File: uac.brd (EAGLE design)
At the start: 160 x 100 mm, 158 parts, among them Q1 2N7002CK4SST

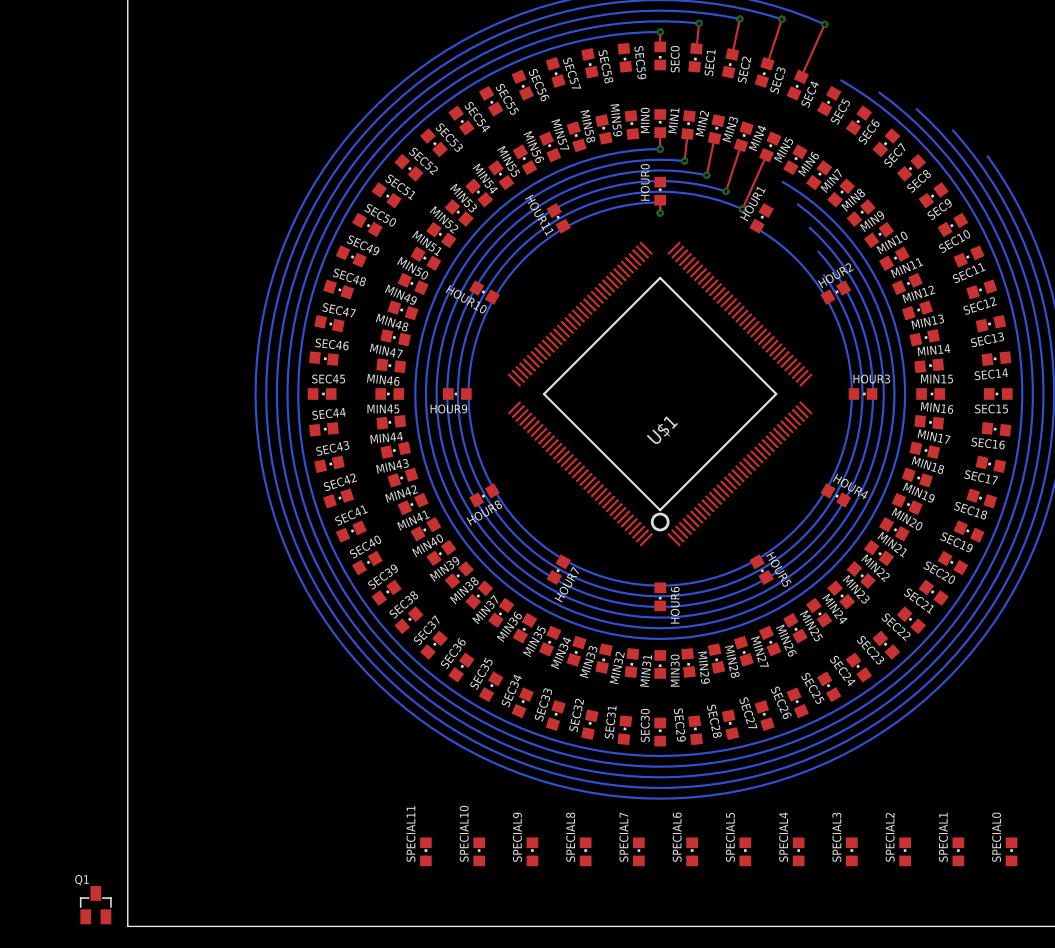
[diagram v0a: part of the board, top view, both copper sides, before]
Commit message: Arcdozen 2 toegevoegd
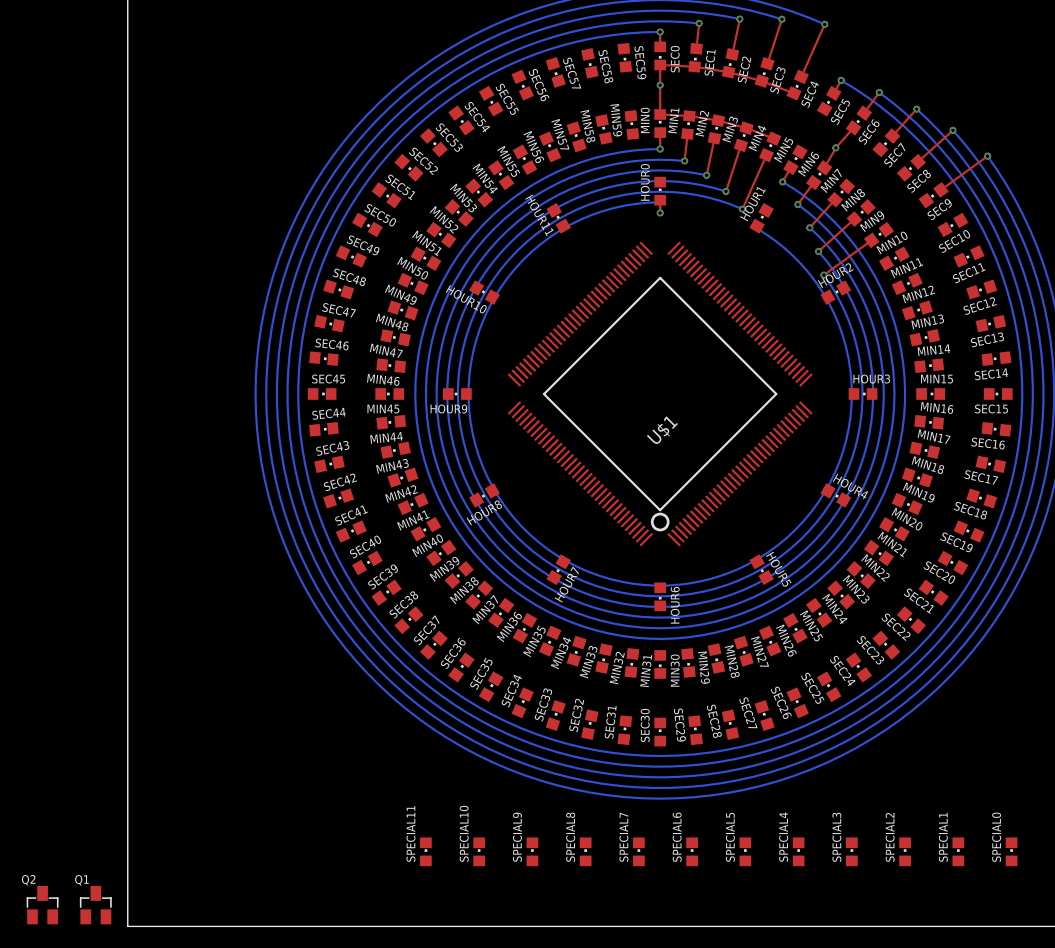
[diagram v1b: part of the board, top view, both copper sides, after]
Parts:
- added Q2: 2N7002CK4SST, Custom components:SOT23
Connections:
- new net ARCDOZEN_2: Q2.1
- new net N$1: HOUR1.C, MIN5.C, MIN6.C, MIN7.C, MIN8.C, MIN9.C, Q2.3, SEC5.C, SEC6.C, SEC7.C, SEC8.C, SEC9.C, SPECIAL1.C
- net DOZEN1: now also HOUR1.A
- net DOZEN10: now also SEC8.A
- net DOZEN11: now also SEC9.A
- net DOZEN12: now also SPECIAL1.A
- net DOZEN2: now also MIN5.A
- net DOZEN3: now also MIN6.A
- net DOZEN4: now also MIN7.A
- net DOZEN5: now also MIN8.A
- net DOZEN6: now also MIN9.A
- net DOZEN7: now also SEC5.A
- net DOZEN8: now also SEC6.A
- net DOZEN9: now also SEC7.A
- net GND: now also Q2.2
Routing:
- net N$3: track 0.00 -> 28.6 mm, vias 0 -> 1
- net DOZEN6: track 15.4 -> 20.9 mm, vias 1 -> 2
- net DOZEN11: track 25.1 -> 30.5 mm, vias 1 -> 2
- net N$1: track 0.00 -> 4.67 mm, vias 0 -> 1
- net DOZEN5: track 14.9 -> 19.5 mm, vias 1 -> 2
- net DOZEN10: track 23.6 -> 28.0 mm, vias 1 -> 2
- net DOZEN4: track 14.4 -> 18.0 mm, vias 1 -> 2
- net DOZEN9: track 22.0 -> 25.4 mm, vias 1 -> 2
- net DOZEN3: track 13.9 -> 16.5 mm, vias 1 -> 2
- net DOZEN8: track 20.5 -> 22.9 mm, vias 1 -> 2
- net DOZEN2: track 13.5 -> 15.0 mm, vias 1 -> 2
- net DOZEN7: track 19.0 -> 20.4 mm, vias 1 -> 2

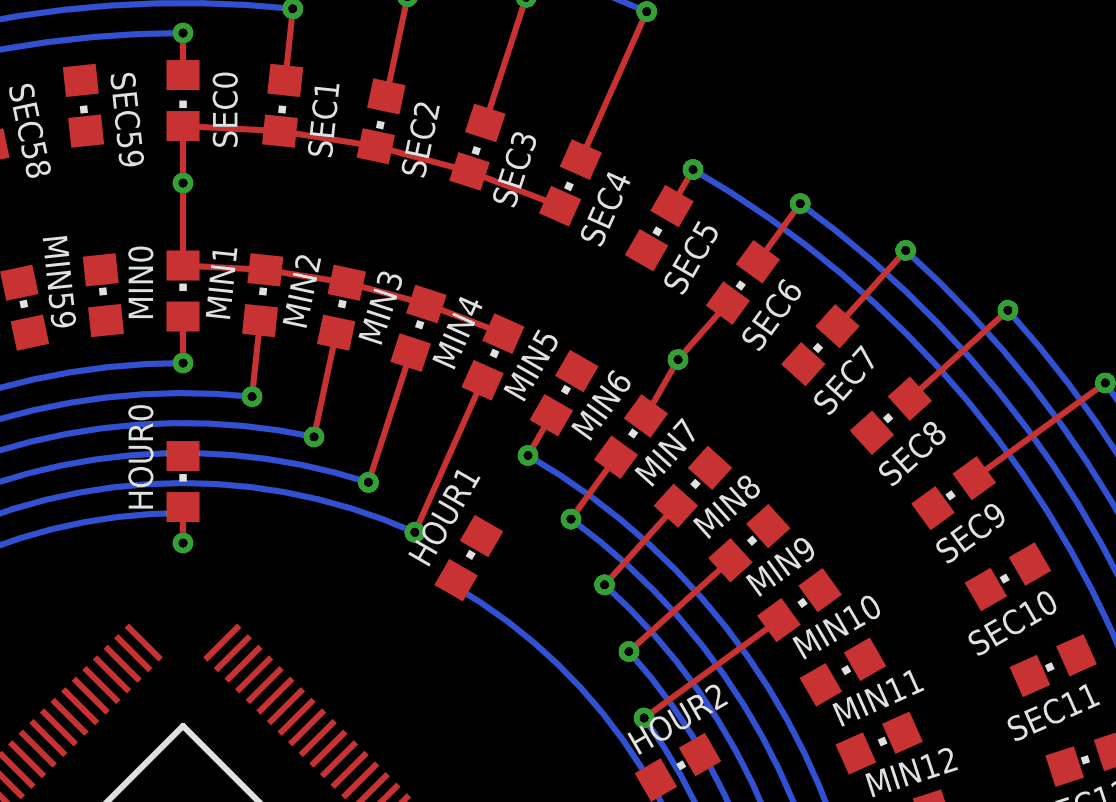
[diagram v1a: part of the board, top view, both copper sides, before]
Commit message: Arcdozen arc
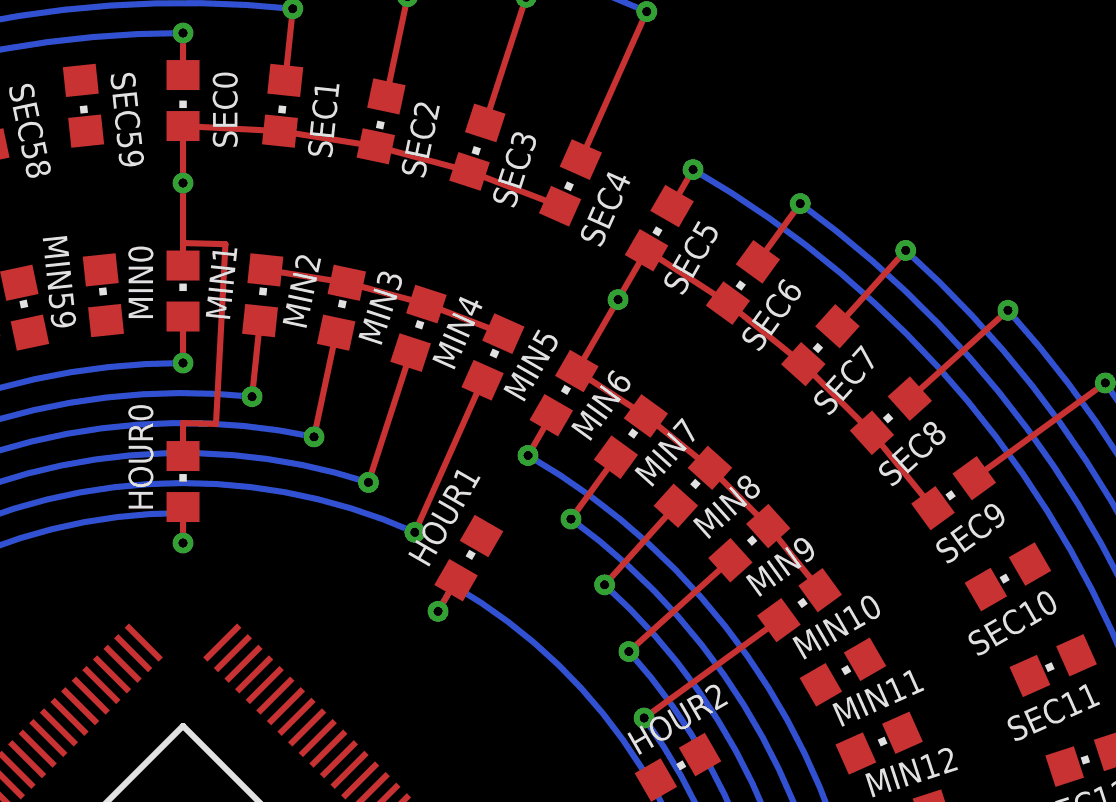
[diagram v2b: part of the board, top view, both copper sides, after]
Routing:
- net N$1: track 4.67 -> 28.7 mm
- net N$3: track 28.6 -> 35.4 mm
- net DOZEN1: track 11.5 -> 13.7 mm, vias 1 -> 2
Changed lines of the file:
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@@
 <layer number="43" name="vRestrict" color="2" fill="10" visible="yes" active="yes"/>
 <layer number="44" name="Drills" color="7" fill="1" visible="no" active="yes"/>
-<layer number="45" name="Holes" color="7" fill="1" visible="no" active="yes"/>
+<layer number="45" name="Holes" color="7" fill="1" visible="yes" active="yes"/>
 <layer number="46" name="Milling" color="3" fill="1" visible="no" active="yes"/>
 <layer number="47" name="Measures" color="7" fill="1" visible="no" active="yes"/>
@@
 <wire x1="55.4576875" y1="75.676384375" x2="58.11169375" y2="74.96524375" width="0.2032" layer="1"/>
 <wire x1="58.11169375" y1="74.96524375" x2="60.67684375" y2="73.98055625" width="0.2032" layer="1"/>
-<wire x1="50" y1="76.25" x2="50" y2="79" width="0.2032" layer="1"/>
+<wire x1="50" y1="76.25" x2="50" y2="77" width="0.2032" layer="1"/>
+<wire x1="50" y1="77" x2="50" y2="79" width="0.2032" layer="1"/>
 <wire x1="50" y1="79" x2="50" y2="80.9" width="0.2032" layer="1"/>
-<wire x1="50" y1="76.25" x2="52.743859375" y2="76.1062" width="0.2032" layer="1"/>
 <via x="50" y="79" extent="1-16" drill="0.3"/>
-<wire x1="50" y1="69.9" x2="50" y2="76.25" width="0" layer="19" extent="1-1"/>
+<wire x1="50" y1="69.9" x2="50" y2="71" width="0.2032" layer="1"/>
+<wire x1="50" y1="71" x2="51.09905625" y2="70.97121875" width="0.2032" layer="1"/>
+<wire x1="51.09905625" y1="70.97121875" x2="51.413071875" y2="76.962996875" width="0.2032" layer="1"/>
+<wire x1="51.413071875" y1="76.962996875" x2="50" y2="77" width="0.2032" layer="1"/>
+<wire x1="51.413071875" y1="76.962996875" x2="52.743859375" y2="76.1062" width="0" layer="19" extent="1-1"/>
 <wire x1="83" y1="7.85" x2="60.67684375" y2="73.98055625" width="0" layer="19" extent="1-1"/>
 <wire x1="-3" y1="3.1" x2="50" y2="69.9" width="0" layer="19" extent="1-1"/>
@@
 <wire x1="50" y1="67" x2="50" y2="68" width="0.2032" layer="16"/>
 <contactref element="HOUR1" pad="A"/>
+<wire x1="59" y1="65.588459375" x2="58.5" y2="64.72243125" width="0.2032" layer="16"/>
+<via x="58.5" y="64.72243125" extent="1-16" drill="0.3"/>
+<wire x1="58.5" y1="64.72243125" x2="59.1" y2="65.761659375" width="0.2032" layer="1"/>
 <wire x1="50" y1="68.2" x2="36" y2="96.15" width="0" layer="19" extent="1-1"/>
-<wire x1="59.1" y1="65.761659375" x2="59" y2="65.588459375" width="0" layer="19" extent="1-16"/>
 </signal>
 <signal name="DOZEN2">
@@
 <contactref element="SEC9" pad="C"/>
 <contactref element="Q2" pad="3"/>
-<wire x1="65.429353125" y1="71.23669375" x2="66.5" y2="73.114740625" width="0.2032" layer="1"/>
-<via x="66.5" y="73.114740625" extent="1-16" drill="0.3"/>
-<wire x1="66.5" y1="73.114740625" x2="68.162575" y2="74.99861875" width="0.2032" layer="1"/>
-<wire x1="68.162575" y1="74.99861875" x2="65.45" y2="76.760190625" width="0" layer="19" extent="1-1"/>
-<wire x1="67.5646875" y1="69.50755625" x2="65.429353125" y2="71.23669375" width="0" layer="19" extent="1-1"/>
-<wire x1="69.50755625" y1="67.5646875" x2="67.5646875" y2="69.50755625" width="0" layer="19" extent="1-1"/>
-<wire x1="71.23669375" y1="65.429353125" x2="69.50755625" y2="67.5646875" width="0" layer="19" extent="1-1"/>
-<wire x1="63.125" y1="72.733153125" x2="65.429353125" y2="71.23669375" width="0" layer="19" extent="1-1"/>
-<wire x1="70.676128125" y1="72.963171875" x2="68.162575" y2="74.99861875" width="0" layer="19" extent="1-1"/>
-<wire x1="72.963171875" y1="70.676128125" x2="70.676128125" y2="72.963171875" width="0" layer="19" extent="1-1"/>
-<wire x1="74.99861875" y1="68.162575" x2="72.963171875" y2="70.676128125" width="0" layer="19" extent="1-1"/>
+<via x="64.5" y="75.114740625" extent="1-16" drill="0.3"/>
+<wire x1="65.45" y1="76.760190625" x2="64.57531875" y2="75.245190625" width="0.2032" layer="1"/>
+<wire x1="64.57531875" y1="75.245190625" x2="63.125" y2="72.733153125" width="0.2032" layer="1"/>
+<wire x1="64.5" y1="75.114740625" x2="64.57531875" y2="75.245190625" width="0.2032" layer="1"/>
+<wire x1="65.45" y1="76.760190625" x2="68.162575" y2="74.99861875" width="0.2032" layer="1"/>
+<wire x1="68.162575" y1="74.99861875" x2="70.676128125" y2="72.963171875" width="0.2032" layer="1"/>
+<wire x1="70.676128125" y1="72.963171875" x2="72.963171875" y2="70.676128125" width="0.2032" layer="1"/>
+<wire x1="72.963171875" y1="70.676128125" x2="74.99861875" y2="68.162575" width="0.2032" layer="1"/>
+<wire x1="63.125" y1="72.733153125" x2="65.429353125" y2="71.23669375" width="0.2032" layer="1"/>
+<wire x1="65.429353125" y1="71.23669375" x2="67.5646875" y2="69.50755625" width="0.2032" layer="1"/>
+<wire x1="67.5646875" y1="69.50755625" x2="69.50755625" y2="67.5646875" width="0.2032" layer="1"/>
+<wire x1="69.50755625" y1="67.5646875" x2="71.23669375" y2="65.429353125" width="0.2032" layer="1"/>
 <wire x1="59.95" y1="67.2339" x2="63.125" y2="72.733153125" width="0" layer="19" extent="1-1"/>
 <wire x1="78" y1="7.85" x2="71.23669375" y2="65.429353125" width="0" layer="19" extent="1-1"/>

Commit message: arcdozen2
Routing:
- net N$1: track 28.7 -> 18.8 mm
- net N$3: track 35.4 -> 44.8 mm
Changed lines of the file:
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@@
 <contactref element="Q1" pad="3"/>
 <contactref element="SPECIAL0" pad="C"/>
-<wire x1="50" y1="80.9" x2="53.229940625" y2="80.730715625" width="0.2032" layer="1"/>
-<wire x1="53.229940625" y1="80.730715625" x2="56.42448125" y2="80.224771875" width="0.2032" layer="1"/>
-<wire x1="56.42448125" y1="80.224771875" x2="59.54861875" y2="79.387653125" width="0.2032" layer="1"/>
-<wire x1="59.54861875" y1="79.387653125" x2="62.568165625" y2="78.22855625" width="0.2032" layer="1"/>
-<wire x1="52.743859375" y1="76.1062" x2="55.4576875" y2="75.676384375" width="0.2032" layer="1"/>
-<wire x1="55.4576875" y1="75.676384375" x2="58.11169375" y2="74.96524375" width="0.2032" layer="1"/>
-<wire x1="58.11169375" y1="74.96524375" x2="60.67684375" y2="73.98055625" width="0.2032" layer="1"/>
-<wire x1="50" y1="76.25" x2="50" y2="77" width="0.2032" layer="1"/>
-<wire x1="50" y1="77" x2="50" y2="79" width="0.2032" layer="1"/>
-<wire x1="50" y1="79" x2="50" y2="80.9" width="0.2032" layer="1"/>
-<via x="50" y="79" extent="1-16" drill="0.3"/>
-<wire x1="50" y1="69.9" x2="50" y2="71" width="0.2032" layer="1"/>
-<wire x1="50" y1="71" x2="51.09905625" y2="70.97121875" width="0.2032" layer="1"/>
-<wire x1="51.09905625" y1="70.97121875" x2="51.413071875" y2="76.962996875" width="0.2032" layer="1"/>
-<wire x1="51.413071875" y1="76.962996875" x2="50" y2="77" width="0.2032" layer="1"/>
-<wire x1="51.413071875" y1="76.962996875" x2="52.743859375" y2="76.1062" width="0" layer="19" extent="1-1"/>
+<wire x1="50" y1="76.25" x2="50" y2="78.5" width="0.2032" layer="1"/>
+<wire x1="50" y1="78.5" x2="50" y2="80.9" width="0.2032" layer="1"/>
+<via x="50" y="78.5" extent="1-16" drill="0.3"/>
+<wire x1="61.59199375" y1="76.036046875" x2="51.491575" y2="78.460940625" width="0.2032" layer="1" curve="20.999995"/>
+<wire x1="51.491575" y1="78.460940625" x2="50" y2="78.5" width="0.2032" layer="1" curve="3"/>
+<wire x1="53.229940625" y1="80.730715625" x2="52.743859375" y2="76.1062" width="0.2032" layer="1"/>
+<wire x1="56.42448125" y1="80.224771875" x2="55.4576875" y2="75.676384375" width="0.2032" layer="1"/>
+<wire x1="59.54861875" y1="79.387653125" x2="58.11169375" y2="74.96524375" width="0.2032" layer="1"/>
+<wire x1="62.568165625" y1="78.22855625" x2="60.67684375" y2="73.98055625" width="0.2032" layer="1"/>
+<wire x1="50" y1="69.9" x2="50" y2="70" width="0.2032" layer="1"/>
+<wire x1="51.04671875" y1="69.972590625" x2="50" y2="70" width="0.2032" layer="1" curve="2.999999"/>
+<wire x1="51.04671875" y1="69.972590625" x2="51.491575" y2="78.460940625" width="0.2032" layer="1"/>
+<wire x1="61.59199375" y1="76.036046875" x2="60.67684375" y2="73.98055625" width="0" layer="19" extent="1-1"/>
+<wire x1="52.743859375" y1="76.1062" x2="51.491575" y2="78.460940625" width="0" layer="19" extent="1-1"/>
+<wire x1="58.11169375" y1="74.96524375" x2="60.67684375" y2="73.98055625" width="0" layer="19" extent="1-1"/>
+<wire x1="55.4576875" y1="75.676384375" x2="52.743859375" y2="76.1062" width="0" layer="19" extent="1-1"/>
 <wire x1="83" y1="7.85" x2="60.67684375" y2="73.98055625" width="0" layer="19" extent="1-1"/>
 <wire x1="-3" y1="3.1" x2="50" y2="69.9" width="0" layer="19" extent="1-1"/>
@@
 <contactref element="SEC9" pad="C"/>
 <contactref element="Q2" pad="3"/>
-<via x="64.5" y="75.114740625" extent="1-16" drill="0.3"/>
-<wire x1="65.45" y1="76.760190625" x2="64.57531875" y2="75.245190625" width="0.2032" layer="1"/>
-<wire x1="64.57531875" y1="75.245190625" x2="63.125" y2="72.733153125" width="0.2032" layer="1"/>
-<wire x1="64.5" y1="75.114740625" x2="64.57531875" y2="75.245190625" width="0.2032" layer="1"/>
-<wire x1="65.45" y1="76.760190625" x2="68.162575" y2="74.99861875" width="0.2032" layer="1"/>
-<wire x1="68.162575" y1="74.99861875" x2="70.676128125" y2="72.963171875" width="0.2032" layer="1"/>
-<wire x1="70.676128125" y1="72.963171875" x2="72.963171875" y2="70.676128125" width="0.2032" layer="1"/>
-<wire x1="72.963171875" y1="70.676128125" x2="74.99861875" y2="68.162575" width="0.2032" layer="1"/>
-<wire x1="63.125" y1="72.733153125" x2="65.429353125" y2="71.23669375" width="0.2032" layer="1"/>
-<wire x1="65.429353125" y1="71.23669375" x2="67.5646875" y2="69.50755625" width="0.2032" layer="1"/>
-<wire x1="67.5646875" y1="69.50755625" x2="69.50755625" y2="67.5646875" width="0.2032" layer="1"/>
-<wire x1="69.50755625" y1="67.5646875" x2="71.23669375" y2="65.429353125" width="0.2032" layer="1"/>
+<via x="64.25" y="74.681725" extent="1-16" drill="0.3"/>
+<wire x1="63.125" y1="72.733153125" x2="65.45" y2="76.760190625" width="0.2032" layer="1"/>
+<wire x1="70.676128125" y1="72.963171875" x2="68.162575" y2="74.99861875" width="0" layer="19" extent="1-1"/>
+<wire x1="72.963171875" y1="70.676128125" x2="70.676128125" y2="72.963171875" width="0" layer="19" extent="1-1"/>
+<wire x1="74.99861875" y1="68.162575" x2="72.963171875" y2="70.676128125" width="0" layer="19" extent="1-1"/>
+<wire x1="65.45" y1="76.760190625" x2="68.162575" y2="74.99861875" width="0" layer="19" extent="1-1"/>
+<wire x1="65.429353125" y1="71.23669375" x2="63.125" y2="72.733153125" width="0" layer="19" extent="1-1"/>
+<wire x1="67.5646875" y1="69.50755625" x2="65.429353125" y2="71.23669375" width="0" layer="19" extent="1-1"/>
+<wire x1="69.50755625" y1="67.5646875" x2="67.5646875" y2="69.50755625" width="0" layer="19" extent="1-1"/>
+<wire x1="71.23669375" y1="65.429353125" x2="69.50755625" y2="67.5646875" width="0" layer="19" extent="1-1"/>
 <wire x1="59.95" y1="67.2339" x2="63.125" y2="72.733153125" width="0" layer="19" extent="1-1"/>
 <wire x1="78" y1="7.85" x2="71.23669375" y2="65.429353125" width="0" layer="19" extent="1-1"/>
 <wire x1="-8" y1="3.1" x2="78" y2="7.85" width="0" layer="19" extent="1-1"/>
+<wire x1="64.25" y1="74.681725" x2="63.125" y2="72.733153125" width="0.2032" layer="1"/>
+<wire x1="73.056984375" y1="66.75188125" x2="64.25" y2="74.681725" width="0.2032" layer="1" curve="23.999999"/>
 </signal>
 <signal name="ARCDOZEN_2">

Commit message: arcdozen2
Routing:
- net N$1: track 18.8 -> 37.4 mm
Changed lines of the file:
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@@
 <via x="64.25" y="74.681725" extent="1-16" drill="0.3"/>
 <wire x1="63.125" y1="72.733153125" x2="65.45" y2="76.760190625" width="0.2032" layer="1"/>
-<wire x1="70.676128125" y1="72.963171875" x2="68.162575" y2="74.99861875" width="0" layer="19" extent="1-1"/>
-<wire x1="72.963171875" y1="70.676128125" x2="70.676128125" y2="72.963171875" width="0" layer="19" extent="1-1"/>
-<wire x1="74.99861875" y1="68.162575" x2="72.963171875" y2="70.676128125" width="0" layer="19" extent="1-1"/>
-<wire x1="65.45" y1="76.760190625" x2="68.162575" y2="74.99861875" width="0" layer="19" extent="1-1"/>
-<wire x1="65.429353125" y1="71.23669375" x2="63.125" y2="72.733153125" width="0" layer="19" extent="1-1"/>
+<wire x1="64.25" y1="74.681725" x2="63.125" y2="72.733153125" width="0.2032" layer="1"/>
+<wire x1="73.056984375" y1="66.75188125" x2="64.25" y2="74.681725" width="0.2032" layer="1" curve="23.999999"/>
+<wire x1="68.162575" y1="74.99861875" x2="65.429353125" y2="71.23669375" width="0.2032" layer="1"/>
+<wire x1="70.676128125" y1="72.963171875" x2="67.5646875" y2="69.50755625" width="0.2032" layer="1"/>
+<wire x1="72.963171875" y1="70.676128125" x2="69.50755625" y2="67.5646875" width="0.2032" layer="1"/>
+<wire x1="74.99861875" y1="68.162575" x2="71.23669375" y2="65.429353125" width="0.2032" layer="1"/>
 <wire x1="67.5646875" y1="69.50755625" x2="65.429353125" y2="71.23669375" width="0" layer="19" extent="1-1"/>
 <wire x1="69.50755625" y1="67.5646875" x2="67.5646875" y2="69.50755625" width="0" layer="19" extent="1-1"/>
 <wire x1="71.23669375" y1="65.429353125" x2="69.50755625" y2="67.5646875" width="0" layer="19" extent="1-1"/>
+<wire x1="73.056984375" y1="66.75188125" x2="71.23669375" y2="65.429353125" width="0" layer="19" extent="1-1"/>
 <wire x1="59.95" y1="67.2339" x2="63.125" y2="72.733153125" width="0" layer="19" extent="1-1"/>
 <wire x1="78" y1="7.85" x2="71.23669375" y2="65.429353125" width="0" layer="19" extent="1-1"/>
 <wire x1="-8" y1="3.1" x2="78" y2="7.85" width="0" layer="19" extent="1-1"/>
-<wire x1="64.25" y1="74.681725" x2="63.125" y2="72.733153125" width="0.2032" layer="1"/>
-<wire x1="73.056984375" y1="66.75188125" x2="64.25" y2="74.681725" width="0.2032" layer="1" curve="23.999999"/>
 </signal>
 <signal name="ARCDOZEN_2">
